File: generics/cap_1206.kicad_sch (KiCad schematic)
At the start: 0 parts

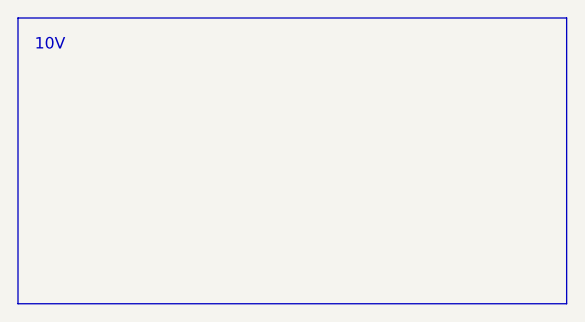
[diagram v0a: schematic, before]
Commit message: Add parts for starter motor
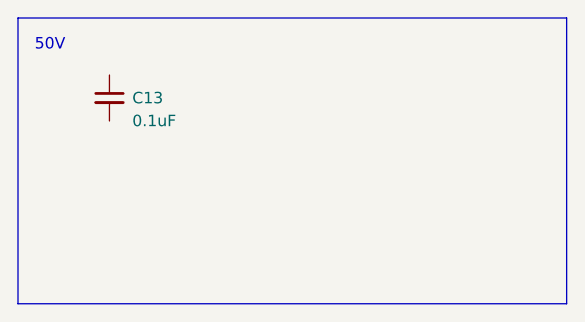
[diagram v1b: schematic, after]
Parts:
- added C13: 0.1uF, Capacitor_SMD:C_0805_2012Metric, symbol Device:C_Small
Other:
- note added: "50V"
- note removed: "10V"
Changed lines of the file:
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@@
 		)
 	)
-	(text "10V"
+	(text "50V"
 		(exclude_from_sim no)
 		(at 31.496 25.908 0)
@@
 			)
 		)
+	)
+	(symbol
+		(lib_id "Device:C_Small")
+		(at 38.1 31.75 0)
+		(mirror y)
+		(unit 1)
+		(exclude_from_sim no)
+		(in_bom yes)
+		(on_board yes)
+		(dnp no)
+		(property "Reference" "C13"
+			(at 40.64 31.75 0)
+			(effects
+				(font
+					(size 1.27 1.27)
+				)
+				(justify right)
+			)
+		)
+		(property "Value" "0.1uF"
+			(at 40.64 34.29 0)
+			(effects
+				(font
+					(size 1.27 1.27)
+				)
+				(justify right)
+			)
+		)
+		(property "Footprint" "Capacitor_SMD:C_0805_2012Metric"
+			(at 38.1 31.75 0)
+			(effects
+				(font
+					(size 1.27 1.27)
+				)
+				(hide yes)
+			)
+		)
+		(property "Datasheet" "~"
+			(at 38.1 31.75 0)
+			(effects
+				(font
+					(size 1.27 1.27)
+				)
+				(hide yes)
+			)
+		)
+		(property "Description" "Unpolarized capacitor, small symbol"
+			(at 38.1 31.75 0)
+			(effects
+				(font
+					(size 1.27 1.27)
+				)
+				(hide yes)
+			)
+		)
+		(property "MPN" "CL31B224KBFNNNE"
+			(at 38.1 31.75 0)
+			(effects
+				(font
+					(size 1.27 1.27)
+				)
+				(hide yes)
+			)
+		)
+		(property "Mfr" "Samsung"
+			(at 38.1 31.75 0)
+			(effects
+				(font
+					(size 1.27 1.27)
+				)
+				(hide yes)
+			)
+		)
+		(property "JLCPCB_PN" "C318764"
+			(at 38.1 31.75 0)
+			(effects
+				(font
+					(size 1.27 1.27)
+				)
+				(hide yes)
+			)
+		)
+		(property "Package" "1206"
+			(at 38.1 31.75 0)
+			(effects
+				(font
+					(size 1.27 1.27)
+				)
+				(hide yes)
+			)
+		)
+		(property "Voltage" "50V"
+			(at 38.1 31.75 0)
+			(effects
+				(font
+					(size 1.27 1.27)
+				)
+				(hide yes)
+			)
+		)
+		(property "Tolerance" "10%"
+			(at 38.1 31.75 0)
+			(effects
+				(font
+					(size 1.27 1.27)
+				)
+				(hide yes)
+			)
+		)
+		(property "Dielectric_Class" "X7R"
+			(at 38.1 31.75 0)
+			(effects
+				(font
+					(size 1.27 1.27)
+				)
+				(hide yes)
+			)
+		)
+		(pin "2"
+		)
+		(pin "1"
+		)
+		(instances
+			(project "generics"
+				(path "/ff075d90-2677-48ca-91fd-a3a441ca4e63/fd31fcbb-3763-4427-bc93-82ea9abded6b"
+					(reference "C13")
+					(unit 1)
+				)
+			)
+		)
